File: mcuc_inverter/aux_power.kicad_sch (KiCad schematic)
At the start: 122 parts, among them Q601 CSD18543Q3A-class [TBV], Q602 CSD18543Q3A-class [TBV], Q603 CSD18543Q3A-class [TBV], Q604 CSD18543Q3A-class [TBV], Q605 CSD18543Q3A-class [TBV], T601 custom flyback, Lp<500uH, VOR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, T602 750316856, T603 750316856, T604 750316856, T605 750316856, U601 INN3990CQ, U603 LM5175RHFR, U604 LM74610QDGKRQ1, U605 LMR51430XDDCR, U606 LMR51430XDDCR, U607 TLV1117-33, U608 NXE2S0505MC, U609 SN6505BDBVR, U610 SN6505BDBVR, U611 SN6505BDBVR, U612 SN6505BDBVR

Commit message: Close last footprint TBDs: inductors verified, flyback on EQ30
L601 Bourns SRP6060FA-100M (10uH/7.6A), L602 SRP5030TA-4R7M, L603
SRR1260-120M - all stocked, official KiCad footprints verified on
disk. Rejected: Wuerth 744771110 (P/N does not exist - another
fabrication trap), 744771112 (0 stock/28wk), Coilcraft XAL (delisted
from DigiKey).

T601: DER-948Q's authoritative material list specifies Ferroxcube
EQ30+PLT30/3C96 on MyCoilTech MCT-EIQ3001 bobbin (not the EFD25 its
BOM text mentions) - Lp 422.6uH verified < 500uH (D020), 25T/2T/2T,
and it IS a 15V design so the VOR-raised TBV note is obsolete.
Symbol renumbered to bobbin physical pins dot-for-dot with DER Fig 7
(nets verified identical before/after); footprint T_FLYBACK_EQ30
created (5.0mm pitch rows, 26.8mm row spacing [TBV at RFQ], ~24mm
pri-sec clearance for the reinforced barrier).

ERC 0 errors; zero TBD markers remain in the repo.

Co-Authored-By: Claude Fable 5 <noreply@anthropic.com>
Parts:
- L601: value 10uH [TBV] [FOOTPRINT TBD] -> SRP6060FA-100M 10uH 7.6A; footprint (none) -> Inductor_SMD:L_Bourns_SRP6060FA
- L602: value 4.7uH [TBV] [FOOTPRINT TBD] -> SRP5030TA-4R7M 4.7uH 6A; footprint (none) -> Inductor_SMD:L_Bourns_SRP5030T
- L603: value 12uH [TBV] [FOOTPRINT TBD] -> SRR1260-120M 12uH 5A; footprint (none) -> Inductor_SMD:L_Bourns_SRR1260
- T601: value custom flyback, Lp<500uH, VOR raised for 15 V out [TBV], reinforced >=4kV per SPEC 10 [FOOTPRINT TBD] -> custom flyback per DER-948Q T1: Lp 422.6uH, 25T:2T:2T, 15 V sec, reinforced >=4kV per SPEC 10, core EQ30+PLT30/20/3 3C9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; footprint (none) -> mcuc:T_FLYBACK_EQ30
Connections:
- net DC_BUS_N: now also T601.5 (BIAS-); no longer T601.4 (BIAS-)
- net DC_BUS_P: now also T601.3 (PRI+); no longer T601.1 (PRI+)
- net GND: now also T601.9 (SEC-); no longer T601.6 (SEC-)
- net at D601.2 (A), U601.24 (D): now also T601.1 (PRI-); no longer T601.2 (PRI-)
- net at D603.2 (A), R607.1, R608.1: now also T601.8 (SEC+); no longer T601.5 (SEC+)
- net at D602.2 (A): now also T601.6 (BIAS+); no longer T601.3 (BIAS+)
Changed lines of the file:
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@@
 			)
 		)
-		(property "Value" "custom flyback, Lp<500uH, VOR raised for 15 V out [TBV], reinforced >=4kV per SPEC 10 [FOOTPRINT TBD]"
+		(property "Value" "custom flyback per DER-948Q T1: Lp 422.6uH, 25T:2T:2T, 15 V sec, reinforced >=4kV per SPEC 10, core EQ30+PLT30/20/3 3C96, bobbin MCT-EIQ3001 V4+6P"
 			(at 60.96 33.02 0)
 			(effects
@@
 			)
 		)
-		(property "Footprint" ""
+		(property "Footprint" "mcuc:T_FLYBACK_EQ30"
 			(at 99.06 53.34 0)
 			(effects
@@
 			)
 		)
-		(property "Value" "10uH [TBV] [FOOTPRINT TBD]"
+		(property "Value" "SRP6060FA-100M 10uH 7.6A"
 			(at 120.142 173.99 270)
 			(effects
@@
 			)
 		)
-		(property "Footprint" ""
+		(property "Footprint" "Inductor_SMD:L_Bourns_SRP6060FA"
 			(at 118.11 172.72 0)
 			(effects
@@
 			)
 		)
-		(property "Value" "4.7uH [TBV] [FOOTPRINT TBD]"
+		(property "Value" "SRP5030TA-4R7M 4.7uH 6A"
 			(at 193.80200000000002 222.25 270)
 			(effects
@@
 			)
 		)
-		(property "Footprint" ""
+		(property "Footprint" "Inductor_SMD:L_Bourns_SRP5030T"
 			(at 191.77 220.98 0)
 			(effects
@@
 			)
 		)
-		(property "Value" "12uH [TBV] [FOOTPRINT TBD]"
+		(property "Value" "SRR1260-120M 12uH 5A"
 			(at 193.80200000000002 265.43 270)
 			(effects
@@
 			)
 		)
-		(property "Footprint" ""
+		(property "Footprint" "Inductor_SMD:L_Bourns_SRR1260"
 			(at 191.77 264.16 0)
 			(effects

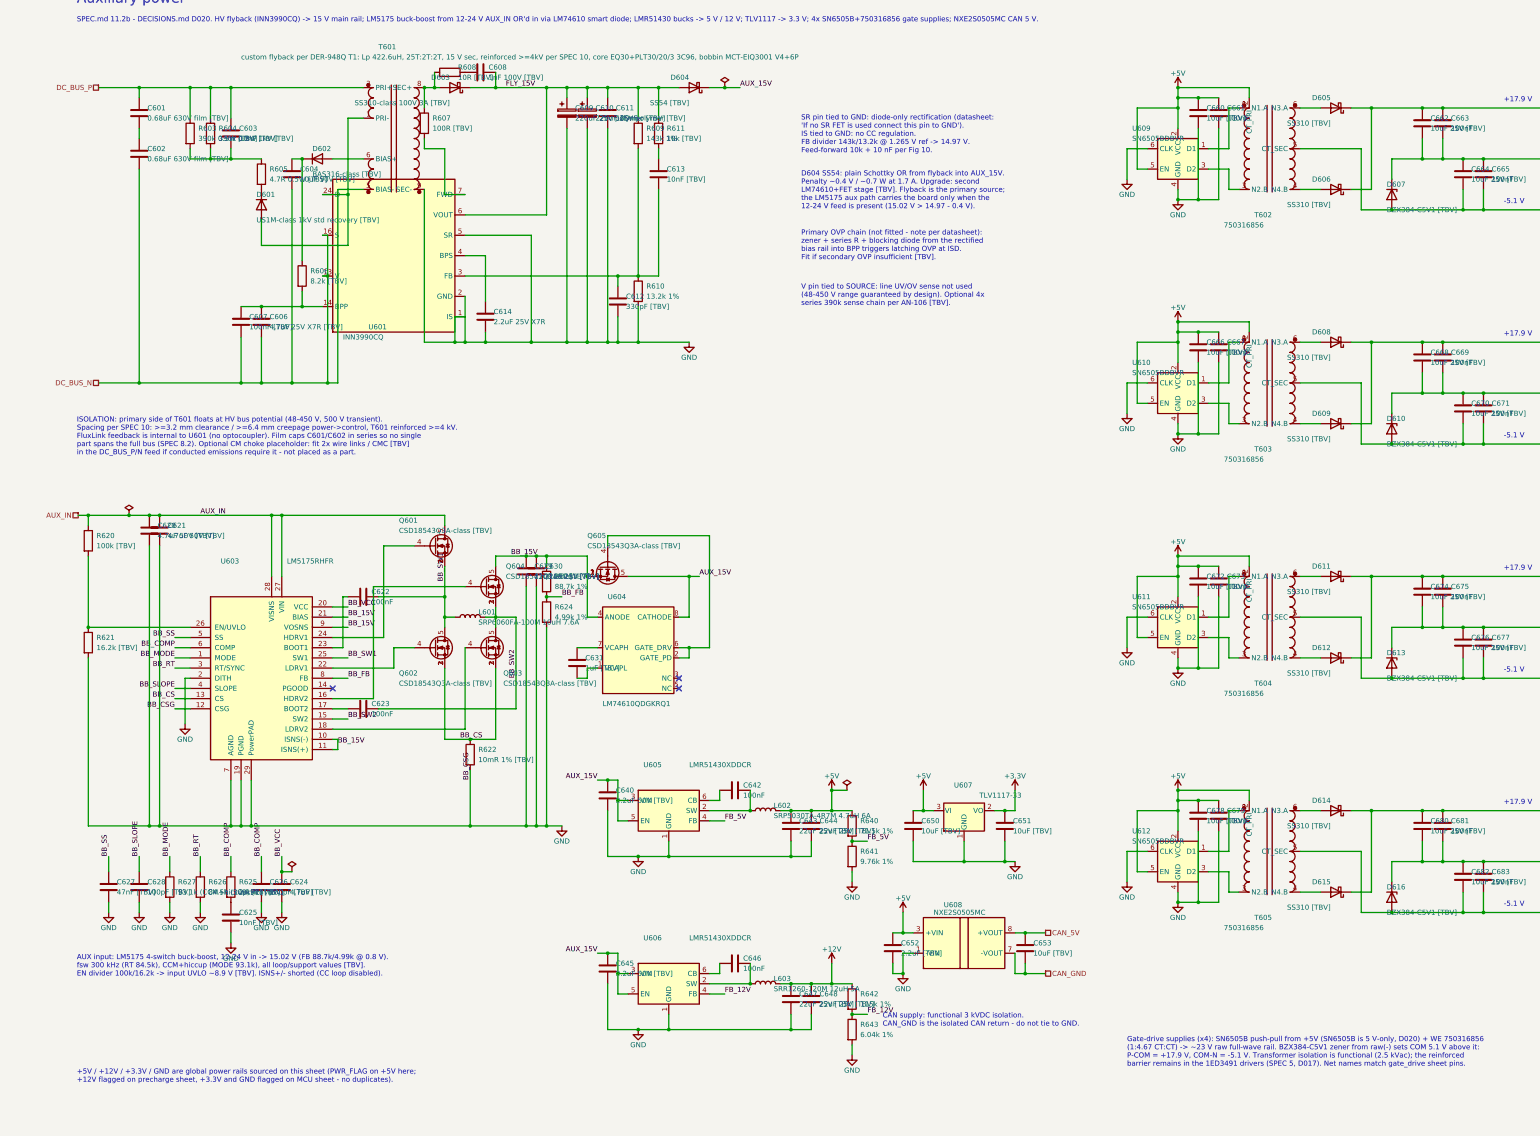
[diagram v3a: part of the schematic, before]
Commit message: Fix aux power and bus sense per adversarial review (CR-4..7, MJ-5..22)
CR-6: real footprints for every HV part that had an impossible one -
C601/C602 (0.68 uF 630 V X2) onto the 26.5x10.5/P22.5 radial box, and
the InnoSwitch bypass caps off 0603 per the datasheet's explicit "0805
or larger, do not use 0603 rated MLCC".

CR-4: RCD clamp rebuilt as 6x 39k 1206 in 3s2p (58.5k) - worst-case
0.35 W and 117 V per part, inside a 200 V 0.5 W part everywhere,
against 0603s that were at 7.5x their voltage rating. Drain lands
731-806 V depending on leakage, so the T601 purchase spec now needs
L_k <= 2 uH; recorded on-sheet.

CR-5 solved better than directed: the agent found the -AQ family has
no reduced current-limit setting, so swapping to INN3999CQ was the
wrong premise. Changing the BPP capacitor 4.7 -> 0.47 uF selects the
standard limit, giving B_pk 360 mT typ (below DER-948Q's own 376 mT
design point) while keeping MORE power headroom than the part swap
would have. Controller retained.

CR-7: both bucks LMR51430 SOT-23-6 -> LMR33630ADDAR HSOIC-8 PowerPAD
(42.9 vs 107.8 C/W), new verified symbol, thermal pad wired as AGND
per Table 6-1. Dividers, 10 uH inductors and 10 uF + 220 nF input
capacitance per Table 9-2.

MJ-14: flyback line UV/OV sensing enabled (the V pin was tied to
SOURCE, which the reference design warns makes regulation fail below
80 V while SPEC requires 48 V). Brown-in 32.5-44.2 V over temp.

MJ-10: LM5175 current limit 10 -> 30 mOhm; it was tripping at 17 A
against a 7.6 A inductor saturation, so the inductor saturated before
the limit acted. MJ-5: bus-sense filter 100 nF -> 100 pF, moving the
OVP response from ~1.3 ms to ~13 us. MJ-16: C702's unconnected pin
wired - it was the LDO output capacitor whose net was never drawn.

MJ-22 deviates from my instruction, correctly: at the gain I specified
the 490 V OVP would have landed 6 mV above a -4% supply rail, i.e.
unreachable by an RRIO output. Gain 1.50 instead - 500 V -> 2.988 V,
90.5% of range, 168 mV hea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
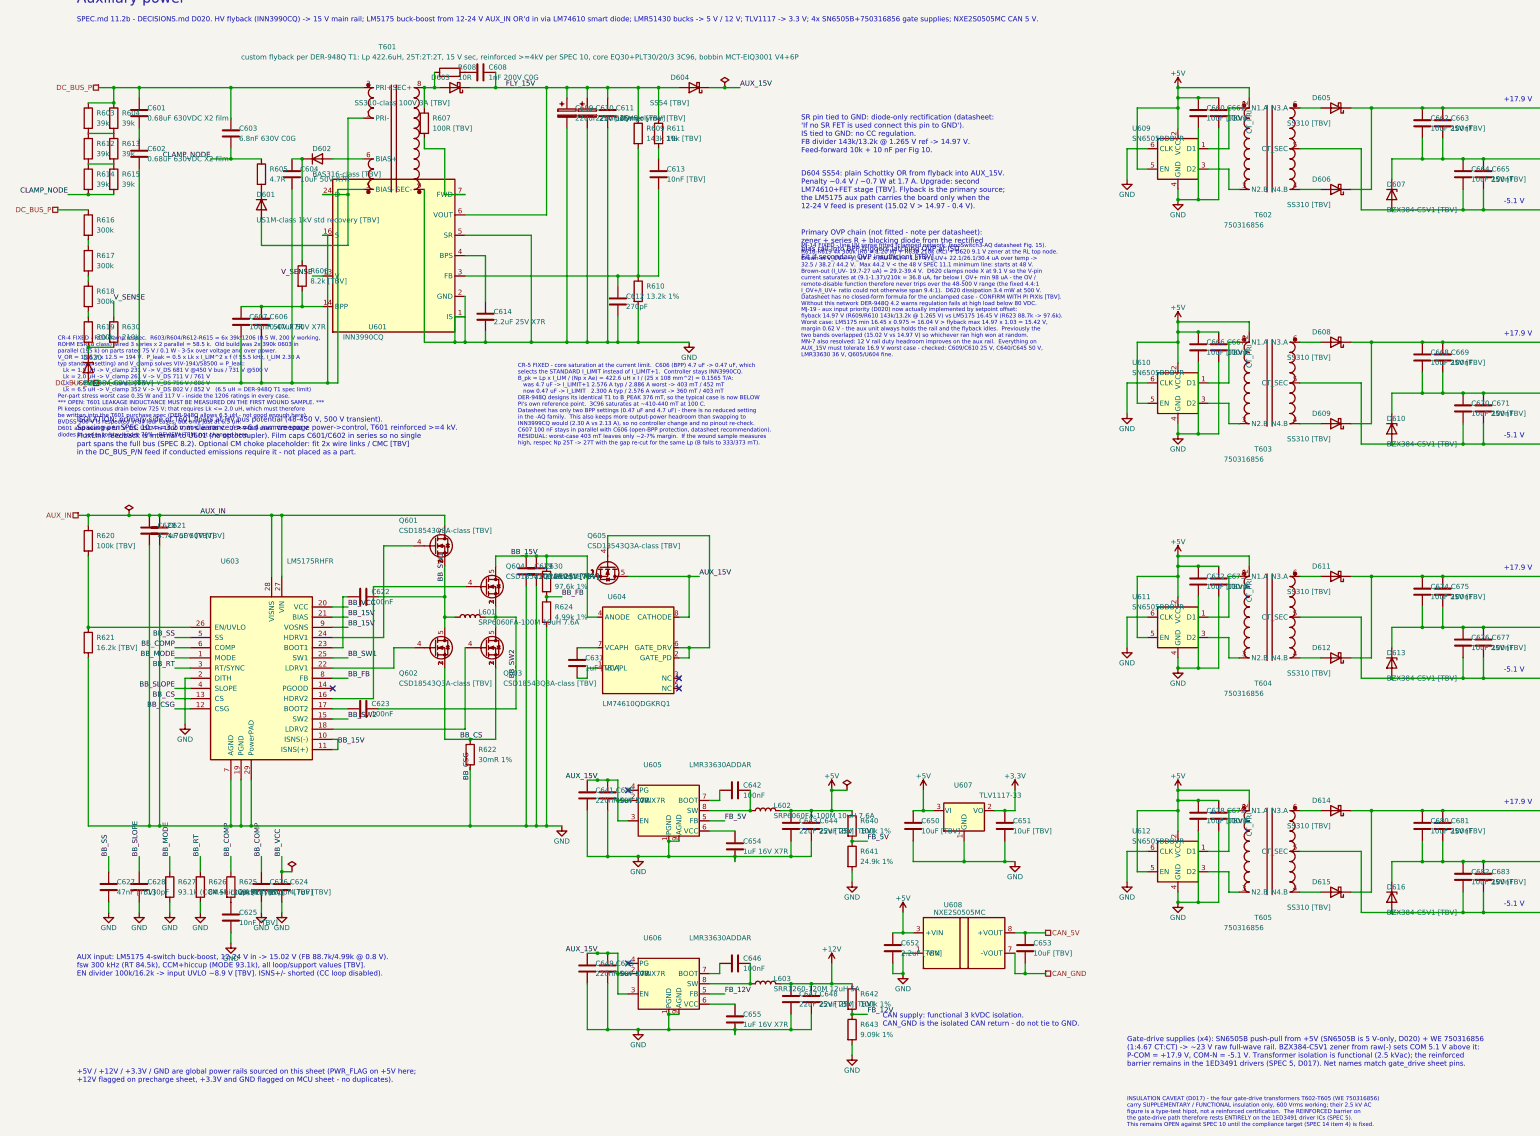
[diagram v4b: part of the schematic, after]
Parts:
- added C641, C649: 220nF 50V X7R, Capacitor_SMD:C_0603_1608Metric, symbol Device:C
- added C654, C655: 1uF 16V X7R, Capacitor_SMD:C_0603_1608Metric, symbol Device:C
- added D620: BZX384-C9V1 [TBV], Diode_SMD:D_SOD-323, symbol Device:D_Zener
- added R612, R613, R614, R615: 39k, Resistor_SMD:R_1206_3216Metric, symbol Device:R
- added R616, R617, R618, R619: 300k, Resistor_SMD:R_1206_3216Metric, symbol Device:R
- added R630: 210k, Resistor_SMD:R_0603_1608Metric, symbol Device:R
- C601, C602: value 0.68uF 630V film [TBV] -> 0.68uF 630VDC X2 film; footprint Capacitor_SMD:C_0603_1608Metric -> Capacitor_THT:C_Rect_L26.5mm_W10.5mm_P22.50mm_MKS4; Rating (none) -> Radial box 26.5 x 16.5 x 10.5 mm, 22.5 mm lead pitch (TDK B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
- C603: value 10nF 1kV [TBV] -> 6.8nF 630V C0G; footprint Capacitor_SMD:C_0603_1608Metric -> Capacitor_SMD:C_1210_3225Metric; Rating (none) -> TDK CGA5H4C0G2J682J115AE (DER-948Q clamp cap)
- C604: value 10uF 50V [TBV] -> 10uF 50V X7R; footprint Capacitor_SMD:C_0603_1608Metric -> Capacitor_SMD:C_1210_3225Metric
- C606: value 4.7uF 25V X7R [TBV] -> 0.47uF 50V X7R; footprint Capacitor_SMD:C_0603_1608Metric -> Capacitor_SMD:C_0805_2012Metric; Rating (none) -> BPP: 0.47uF selects STANDARD ILIMIT (CR-5). 0805 min per da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
- C607: value 100nF [TBV] -> 100nF 50V X7R; footprint Capacitor_SMD:C_0603_1608Metric -> Capacitor_SMD:C_0805_2012Metric
- C608: value 1nF 100V [TBV] -> 1nF 200V C0G; footprint Capacitor_SMD:C_0603_1608Metric -> Capacitor_SMD:C_0805_2012Metric
- C612: value 330pF [TBV] -> 270pF
- C614: footprint Capacitor_SMD:C_0603_1608Metric -> Capacitor_SMD:C_0805_2012Metric; Rating (none) -> BPS: 0805 min per datasheet (>=1.5uF in operation)
- C628: value 100pF [TBV] -> 130pF
- C640, C645: value 2.2uF 50V [TBV] -> 10uF 50V X7R; footprint Capacitor_SMD:C_0805_2012Metric -> Capacitor_SMD:C_1210_3225Metric
- L602: value SRP5030TA-4R7M 4.7uH 6A -> SRP6060FA-100M 10uH 7.6A; footprint Inductor_SMD:L_Bourns_SRP5030T -> Inductor_SMD:L_Bourns_SRP6060FA
- R603, R604: value 390k 0.5W [TBV] -> 39k; footprint Resistor_SMD:R_0603_1608Metric -> Resistor_SMD:R_1206_3216Metric; Rating (none) -> 0.5W 200V working (ROHM ESR18EZPJ393); Tolerance (none) -> 5%
- R605: value 4.7R 0.5W [TBV] -> 4.7R; footprint Resistor_SMD:R_0603_1608Metric -> Resistor_SMD:R_1206_3216Metric; Rating (none) -> 0.5W 200V working (ROHM ESR18EZPJ4R7)
- R608: value 10R [TBV] -> 10R; footprint Resistor_SMD:R_0603_1608Metric -> Resistor_SMD:R_1206_3216Metric; Rating (none) -> 0.5W 200V working (ROHM ESR18EZPJ100); 0.17 W dissipated
- R622: value 10mR 1% [TBV] -> 30mR 1%
- R623: value 88.7k 1% -> 97.6k 1%
- R640: value 71.5k 1% -> 100k 1%
- R641: value 9.76k 1% -> 24.9k 1%
- R642: value 115k 1% -> 100k 1%
- R643: value 6.04k 1% -> 9.09k 1%
- U605, U606: value LMR51430XDDCR -> LMR33630ADDAR; footprint Package_TO_SOT_SMD:SOT-23-6 -> Package_SO:SOIC-8-1EP_3.9x4.9mm_P1.27mm_EP2.95x4.9mm_Mask2.71x3.4mm; symbol Regulator_Switching:LMR51430 -> mcuc:LMR33630ADDA
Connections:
- net AUX_15V: now also U605.2 (VIN), U606.2 (VIN), C641.1, C649.1; no longer U605.5 (EN), U606.5 (EN)
- net DC_BUS_N: now also D620.2 (A); no longer U601.13 (V)
- net DC_BUS_P: now also R616.1
- net FB_12V: now also U606.5 (FB); no longer U606.4 (FB)
- net FB_5V: now also U605.5 (FB); no longer U605.4 (FB)
- net GND: now also U605.9 (AGND), U606.9 (AGND), C641.2, C649.2, C654.2, C655.2
- net at C642.2, L602.1: now also U605.8 (SW); no longer U605.2 (SW)
- net at U605.6 (VCC): now also C654.1; no longer C642.1
- net at R603.2, R604.2: now also R612.1, R613.1; no longer C603.2, R605.1
- net at C646.1: now also U606.7 (BOOT); no longer U606.6 (CB)
- net at C646.2, L603.1: now also U606.8 (SW); no longer U606.2 (SW)
- new net: C642.1, U605.7 (BOOT)
- new net: D620.1 (K), R619.2, R630.2
- new net: R612.2, R613.2, R614.1, R615.1
- new net: R617.2, R618.1
- new net: R618.2, R619.1
- new net: R616.2, R617.1
- new net: C655.1, U606.6 (VCC)
- new net CLAMP_NODE: C603.2, R605.1, R614.2, R615.2
- new net V_SENSE: R630.1, U601.13 (V)
- no-connect marks 3 -> 5
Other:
- note added: "CR-4 FIXED - RCD clamp respec. R603/R604/R612-R615 = 6x 39k 1206 (0.5 W, 200 V working, ROHM ESR18 class) wired 3 series x 2 parallel = 58.5 k. Old build was 2x 390k 0603 in parallel (195 k) on parts rated 75 V / 0.1 W - 3-5x over voltage and over power. V_OR = 15.5 V x 12.5 = 194 V. P_leak = 0.5 x Lk x I_LIM^2 x f (f 55.5 kHz, I_LIM 2.30 A typ standard setting) and V_clamp solves V(V-194)/58500 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"
- note added: "CR-5 FIXED - core saturation at the current limit. C606 (BPP) 4.7 uF -> 0.47 uF, which selects the STANDARD I_LIMIT instead of I_LIMIT+1. Controller stays INN3990CQ. B_pk = Lp x I_LIM / (Np x Ae) = 422.6 uH x I / (25 x 108 mm^2) = 0.1565 T/A: was 4.7 uF -> I_LIMIT+1 2.576 A typ / 2.886 A worst -> 403 mT / 452 mT now 0.47 uF -> I_LIMIT 2.300 A typ / 2.576 A worst -> 360 mT / 403 mT DER-948Q design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"
- note added: "INSULATION CAVEAT (D017) - the four gate-drive transformers T602-T605 (WE 750316856) carry SUPPLEMENTARY / FUNCTIONAL insulation only, 600 Vrms working; their 2.5 kV AC figure is a type-test hipot, not a reinforced certification. The REINFORCED barrier on the gate-drive path therefore rests ENTIRELY on the 1ED3491 driver ICs (SPEC 5). This remains OPEN against SPEC 10 until the compliance target 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"
- note added: "MJ-14 FIXED - line UV sense fitted (clamped network, InnoSwitch3-AQ datasheet Fig. 15). R616-R619 4x 300k (RU = 1.20 M) + R630 210k (RL) + D620 9.1 V zener at the RL top node. Brown-in V_UV+ = I_UV+ x (RU+RL) + 1.37 V; I_UV+ 22.1/26.1/30.4 uA over temp -> 32.5 / 38.2 / 44.2 V. Max 44.2 V < the 48 V SPEC 11.1 minimum line: starts at 48 V. Brown-out (I_UV- 19.7-27 uA) = 29.2-39.4 V. D620 clamps nod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"
- note added: "MJ-19 - aux input priority (D020) now actually implemented by setpoint offset: flyback 14.97 V (R609/R610 143k/13.2k @ 1.265 V) vs LM5175 16.45 V (R623 88.7k -> 97.6k). Worst case: LM5175 min 16.45 x 0.975 = 16.04 V > flyback max 14.97 x 1.03 = 15.42 V, margin 0.62 V - the aux unit always holds the rail and the flyback idles. Previously the two bands overlapped (15.02 V vs 14.97 V) so whichever r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"
- note removed: "V pin tied to SOURCE: line UV/OV sense not used (48-450 V range guaranteed by design). Optional 4x series 390k sense chain per AN-106 [TBV]."
- moved on the sheet: R603, R604
